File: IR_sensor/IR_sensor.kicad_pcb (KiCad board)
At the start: 2 copper layers, 10 parts, among them J1 Signal_out, J2 5V_In, J3 GND, Q1 BPV11F

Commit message: Added new component
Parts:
- added J4: 5V_In, Connector_PinHeader_2.54mm:PinHeader_1x01_P2.54mm_Vertical, F.Cu at (91.3, 62.1)
- added J5: GND, Connector_PinHeader_2.54mm:PinHeader_1x01_P2.54mm_Vertical, F.Cu at (87.1, 73.4)
- added U1: LM311P, IR_sensor_lib:Voltage_comparator, F.Cu at (85.9, 92.1)
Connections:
- CR2 pad 1: GND -> Net-(J5-Pin_1)
- J3 pad 1: GND -> Net-(J3-Pin_1)
- Q1 pad B: Net-(Q1-PadB) -> unconnected-(Q1-PadB)
- Q1 pad E: GND -> Net-(J3-Pin_1)
- R2 pad 2: GND -> Net-(J3-Pin_1)
- R4 pad 1: Net-(J2-Pin_1) -> Net-(J4-Pin_1)

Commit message: Finalized PCB design
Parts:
- added R5: 2.2k, Resistor_THT:R_Axial_DIN0204_L3.6mm_D1.6mm_P5.08mm_Horizontal, F.Cu at (133.3, 72.7)
- added R6: 500, Resistor_THT:R_Axial_DIN0204_L3.6mm_D1.6mm_P5.08mm_Horizontal, F.Cu at (143.8, 78.9)
- R1, R2, R4: footprint Resistor_THT:R_Axial_DIN0207_L6.3mm_D2.5mm_P5.08mm_Vertical -> Resistor_THT:R_Axial_DIN0204_L3.6mm_D1.6mm_P5.08mm_Horizontal
- R3: value 1M Ohm -> 3k; footprint Resistor_THT:R_Axial_DIN0207_L6.3mm_D2.5mm_P5.08mm_Vertical -> Resistor_THT:R_Axial_DIN0204_L3.6mm_D1.6mm_P5.08mm_Horizontal
- moved J4 74.1 mm to (165.1, 67.8)
- moved R4 73.3 mm to (171.6, 65.3), turned to 90 degrees
- moved J5 72.3 mm to (158.2, 60.2)
- moved CR2 60.4 mm to (163.7, 60.2)
- moved U1 54.6 mm to (140.4, 88.7)
- moved R1 50.8 mm to (148.1, 85.8), turned to 90 degrees
- moved CR1 49.8 mm to (147.2, 70.4), turned to -90 degrees
- moved R2 47.7 mm to (147.1, 65.2), turned to 90 degrees
- moved J2 47.3 mm to (147.3, 99.4)
- moved J1 46.8 mm to (141.2, 99.4)
- moved R3 40.1 mm to (138.6, 68.0), turned to 180 degrees
- moved Q1 35.5 mm to (141.0, 60.1), turned to 180 degrees
- moved J3 31.4 mm to (135.1, 99.7)
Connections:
- CR1 pad 2: Net-(J1-Pin_1) -> GND
- J2 pad 1: Net-(J2-Pin_1) -> +5V
- J3 pad 1: Net-(J3-Pin_1) -> GND
- Q1 pad C: Net-(J1-Pin_1) -> GND
- Q1 pad E: Net-(J3-Pin_1) -> GND
- R1 pad 1: Net-(J2-Pin_1) -> +5V
- R1 pad 2: Net-(J1-Pin_1) -> GND
- R2 pad 2: Net-(J3-Pin_1) -> GND
- R3 pad 1: Net-(Q1-PadB) -> +5V
- R3 pad 2: GND -> Net-(U1-IN+)
- U1 pad 1: unconnected-(U1-EMITOUT-Pad1) -> GND
- U1 pad 2: unconnected-(U1-IN+-Pad2) -> Net-(U1-IN+)
- U1 pad 3: unconnected-(U1-IN--Pad3) -> GND
- U1 pad 4: unconnected-(U1-VCC--Pad4) -> GND
- U1 pad 5: unconnected-(U1-BALANCE-Pad5) -> +5V
- U1 pad 7: unconnected-(U1-COLOUT-Pad7) -> Net-(J1-Pin_1)
- U1 pad 8: unconnected-(U1-VCC+-Pad8) -> +5V
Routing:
- net GND: track 0.00 -> 103.5 mm
- net +5V: track 0.00 -> 43.9 mm
- net Net-(J1-Pin_1): track 0.00 -> 23.8 mm
- net Net-(U1-IN+): track 0.00 -> 20.2 mm
- net Net-(J4-Pin_1): track 0.00 -> 7.49 mm
- net Net-(J5-Pin_1): track 0.00 -> 5.53 mm
- net Net-(CR2-Pad2): track 0.00 -> 5.33 mm
- net Net-(CR1-Pad1): track 0.00 -> 5.24 mm
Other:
- board outline added: 44.9 x 51.1 mm

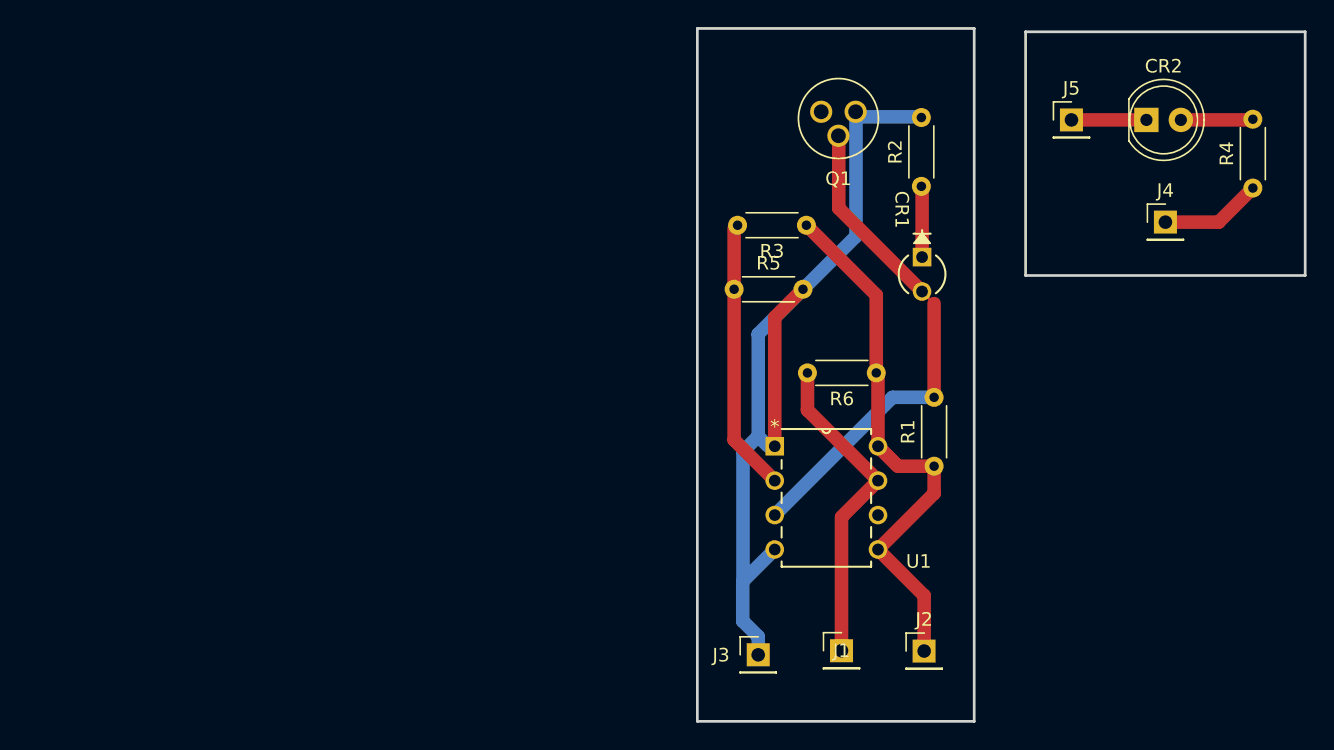
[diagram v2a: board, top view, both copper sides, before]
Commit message: Changed pcb design, added voltage division on output
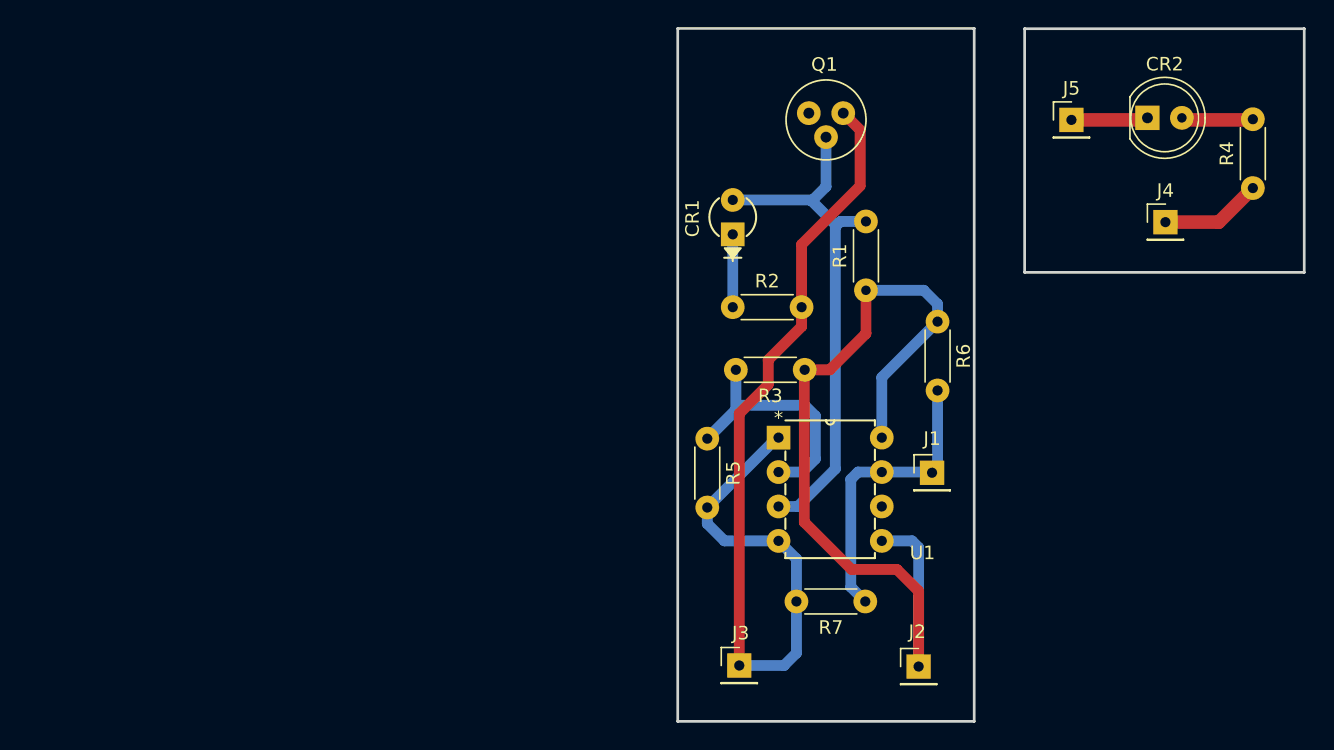
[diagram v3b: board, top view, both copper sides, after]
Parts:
- added R7: 10k, Resistor_THT:R_Axial_DIN0204_L3.6mm_D1.6mm_P5.08mm_Horizontal, F.Cu at (143.0, 95.8)
- R6: value 500 -> 10k
- moved R2 16.5 mm to (133.2, 74.1), turned to 0 degrees
- moved J1 14.7 mm to (147.9, 86.3)
- moved CR1 14.1 mm to (133.2, 68.7), turned to 90 degrees
- moved R1 13.9 mm to (143.0, 72.8)
- moved R5 11.2 mm to (131.3, 83.8), turned to -90 degrees
- moved R3 10.7 mm to (138.5, 78.7)
- moved R6 5.90 mm to (148.3, 75.1), turned to -90 degrees
- moved J3 1.60 mm to (133.7, 100.5)
- moved J2 1.21 mm to (146.9, 100.6)
- moved Q1 0.92 mm to (140.1, 60.2)
- moved U1 0.69 mm to (140.7, 88.1)
- moved CR2 0.17 mm to (163.8, 60.1)
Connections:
- CR1 pad 2: GND -> Net-(U1-IN-)
- Q1 pad C: GND -> Net-(U1-IN-)
- R1 pad 2: GND -> Net-(U1-IN-)
- U1 pad 3: GND -> Net-(U1-IN-)
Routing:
- net Net-(U1-IN-): track 0.00 -> 39.2 mm
- net GND: track 103.5 -> 72.9 mm
- net +5V: track 43.9 -> 65.2 mm
- net Net-(J1-Pin_1): track 23.8 -> 21.9 mm
- net Net-(U1-IN+): track 20.2 -> 21.6 mm
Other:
- board size 44.9 x 51.1 mm -> 46.2 x 51.1 mm
